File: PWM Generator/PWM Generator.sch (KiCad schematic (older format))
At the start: 7 parts

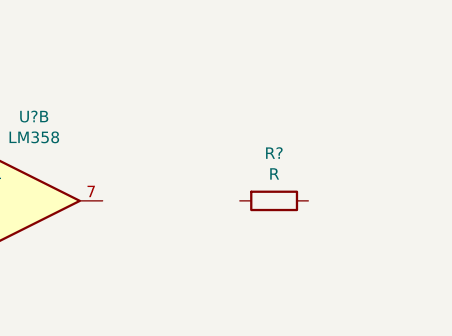
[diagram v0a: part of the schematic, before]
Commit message: Add Diod
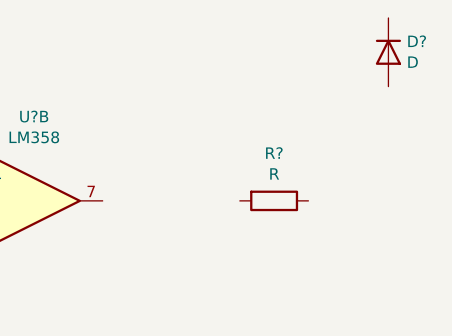
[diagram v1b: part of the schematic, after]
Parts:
- added D?: D, symbol Device:D
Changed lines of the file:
@@
+	0    1    1    0
+$EndComp
+$Comp
+L Device:D D?
+U 1 1 6A953FCE
+P 7900 1000
+F 0 "D?" V 7854 1080 50  0000 L CNN
+F 1 "D" V 7945 1080 50  0000 L CNN
+F 2 "" H 7900 1000 50  0001 C CNN
+F 3 "~" H 7900 1000 50  0001 C CNN
+	1    7900 1000
 	0    1    1    0
 $EndComp

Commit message: wired connection
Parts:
- added C1: C, symbol Device:C
- added C2, C3: CP1, symbol Device:CP1
- added J1, J2: Screw_Terminal_01x02, symbol Connector:Screw_Terminal_01x02
- added Q1: IRF3205, Package_TO_SOT_THT:TO-220-3_Vertical, symbol Transistor_FET:IRF3205
- added RV1: R_POT, symbol Device:R_POT
- added unit 3 of U1
- added U2: LM7805_TO220, Package_TO_SOT_THT:TO-220-3_Vertical, symbol Regulator_Linear:LM7805_TO220
- gave numbers to parts that had none: 7
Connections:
- net at U1.1: now also R3.1, R4.1
- net at U1.2 (-): now also R4.2, U1.5 (+), C1.1
- net at U1.3 (+): now also R1.2, R2.1, R3.2
- net at U1.6 (-): now also RV1.2
- net at U1.7: now also R5.1
- net +12C: now reaches D1.1 (K)
- net +12C: now also C2.1, J1.2 (Pin_2), J2.1 (Pin_1), U2.1 (VI)
- net at D1.2 (A): now also J2.2 (Pin_2), Q1.2 (D)
- net +5V: now reaches R1.1
- net +5V: now also C3.1, RV1.1, U1.8 (V+), U2.3 (VO)
- net GND: now reaches R2.2
- net GND: now also C1.2, C2.2, C3.2, J1.1 (Pin_1), Q1.3 (S), RV1.3, U1.4 (V-), U2.2 (GND)
- net at R5.2: now also Q1.1 (G)
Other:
- moved on the sheet: D1, R1, R2, R3, R4, R5, U1A, U1B

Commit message: PCB net
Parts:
- C1: footprint (none) -> Capacitor_THT:C_Radial_D6.3mm_H5.0mm_P2.50mm
- C2: footprint (none) -> Capacitor_THT:CP_Radial_D10.0mm_P3.50mm
- C3: footprint (none) -> Capacitor_THT:CP_Radial_D7.5mm_P2.50mm
- D1: footprint (none) -> Diode_THT:D_DO-27_P15.24mm_Horizontal
- J1, J2: footprint (none) -> TerminalBlock_4Ucon:TerminalBlock_4Ucon_1x02_P3.50mm_Horizontal
- R1: footprint (none) -> Resistor_THT:R_Radial_Power_L16.1mm_W9.0mm_P7.37mm
- R2, R4, R5: footprint (none) -> Resistor_THT:R_Radial_Power_L11.0mm_W7.0mm_P5.00mm
- R3: footprint (none) -> Resistor_THT:R_Radial_Power_L13.0mm_W9.0mm_P5.00mm
- RV1: footprint (none) -> Potentiometer_THT:Potentiometer_Runtron_RM-065_Vertical
- U1: footprint (none) -> Package_DIP:DIP-8_W7.62mm
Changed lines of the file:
@@
 F 0 "U1" H 3600 2867 50  0000 C CNN
 F 1 "LM358" H 3600 2776 50  0000 C CNN
-F 2 "" H 3600 2500 50  0001 C CNN
+F 2 "Package_DIP:DIP-8_W7.62mm" H 3600 2500 50  0001 C CNN
 F 3 "http://www.ti.com/lit/ds/symlink/lm2904-n.pdf" H 3600 2500 50  0001 C CNN
 	1    3600 2500
@@
 F 0 "U1" H 6150 2767 50  0000 C CNN
 F 1 "LM358" H 6150 2676 50  0000 C CNN
-F 2 "" H 6150 2400 50  0001 C CNN
+F 2 "Package_DIP:DIP-8_W7.62mm" H 6150 2400 50  0001 C CNN
 F 3 "http://www.ti.com/lit/ds/symlink/lm2904-n.pdf" H 6150 2400 50  0001 C CNN
 	2    6150 2400
@@
 F 0 "R4" H 3920 2846 50  0000 L CNN
 F 1 "R" H 3920 2755 50  0000 L CNN
-F 2 "" V 3780 2800 50  0001 C CNN
+F 2 "Resistor_THT:R_Radial_Power_L11.0mm_W7.0mm_P5.00mm" V 3780 2800 50  0001 C CNN
 F 3 "~" H 3850 2800 50  0001 C CNN
 	1    3850 2800
@@
 F 0 "R1" H 2520 2596 50  0000 L CNN
 F 1 "R" H 2520 2505 50  0000 L CNN
-F 2 "" V 2380 2550 50  0001 C CNN
+F 2 "Resistor_THT:R_Radial_Power_L16.1mm_W9.0mm_P7.37mm" V 2380 2550 50  0001 C CNN
 F 3 "~" H 2450 2550 50  0001 C CNN
 	1    2450 2550
@@
 F 0 "R2" H 2520 3146 50  0000 L CNN
 F 1 "R" H 2520 3055 50  0000 L CNN
-F 2 "" V 2380 3100 50  0001 C CNN
+F 2 "Resistor_THT:R_Radial_Power_L11.0mm_W7.0mm_P5.00mm" V 2380 3100 50  0001 C CNN
 F 3 "~" H 2450 3100 50  0001 C CNN
 	1    2450 3100
@@
 F 0 "R5" H 6870 2446 50  0000 L CNN
 F 1 "R" H 6870 2355 50  0000 L CNN
-F 2 "" V 6730 2400 50  0001 C CNN
+F 2 "Resistor_THT:R_Radial_Power_L11.0mm_W7.0mm_P5.00mm" V 6730 2400 50  0001 C CNN
 F 3 "~" H 6800 2400 50  0001 C CNN
 	1    6800 2400
@@
 F 0 "R3" V 2793 2150 50  0000 C CNN
 F 1 "R" V 2884 2150 50  0000 C CNN
-F 2 "" V 2930 2150 50  0001 C CNN
+F 2 "Resistor_THT:R_Radial_Power_L13.0mm_W9.0mm_P5.00mm" V 2930 2150 50  0001 C CNN
 F 3 "~" H 3000 2150 50  0001 C CNN
 	1    3000 2150
@@
 F 0 "D1" V 7404 1880 50  0000 L CNN
 F 1 "D" V 7495 1880 50  0000 L CNN
-F 2 "" H 7450 1800 50  0001 C CNN
+F 2 "Diode_THT:D_DO-27_P15.24mm_Horizontal" H 7450 1800 50  0001 C CNN
 F 3 "~" H 7450 1800 50  0001 C CNN
 	1    7450 1800
@@
 F 0 "C1" H 3315 3396 50  0000 L CNN
 F 1 "C" H 3315 3305 50  0000 L CNN
-F 2 "" H 3238 3200 50  0001 C CNN
+F 2 "Capacitor_THT:C_Radial_D6.3mm_H5.0mm_P2.50mm" H 3238 3200 50  0001 C CNN
 F 3 "~" H 3200 3350 50  0001 C CNN
 	1    3200 3350
@@
 F 0 "C2" H 3815 1396 50  0000 L CNN
 F 1 "CP1" H 3815 1305 50  0000 L CNN
-F 2 "" H 3700 1350 50  0001 C CNN
+F 2 "Capacitor_THT:CP_Radial_D10.0mm_P3.50mm" H 3700 1350 50  0001 C CNN
 F 3 "~" H 3700 1350 50  0001 C CNN
 	1    3700 1350
@@
 F 0 "C3" H 6465 1296 50  0000 L CNN
 F 1 "CP1" H 6465 1205 50  0000 L CNN
-F 2 "" H 6350 1250 50  0001 C CNN
+F 2 "Capacitor_THT:CP_Radial_D7.5mm_P2.50mm" H 6350 1250 50  0001 C CNN
 F 3 "~" H 6350 1250 50  0001 C CNN
 	1    6350 1250
@@
 F 0 "J2" H 9030 1692 50  0000 L CNN
 F 1 "Screw_Terminal_01x02" H 9030 1601 50  0000 L CNN
-F 2 "" H 8950 1700 50  0001 C CNN
+F 2 "TerminalBlock_4Ucon:TerminalBlock_4Ucon_1x02_P3.50mm_Horizontal" H 8950 1700 50  0001 C CNN
 F 3 "~" H 8950 1700 50  0001 C CNN
 	1    8950 1700
@@
 F 0 "J1" H 1518 1725 50  0000 C CNN
 F 1 "Screw_Terminal_01x02" H 1518 1816 50  0000 C CNN
-F 2 "" H 1600 2050 50  0001 C CNN
+F 2 "TerminalBlock_4Ucon:TerminalBlock_4Ucon_1x02_P3.50mm_Horizontal" H 1600 2050 50  0001 C CNN
 F 3 "~" H 1600 2050 50  0001 C CNN
 	1    1600 2050
@@
 F 0 "RV1" H 5081 2646 50  0000 R CNN
 F 1 "R_POT" H 5081 2555 50  0000 R CNN
-F 2 "" H 5150 2600 50  0001 C CNN
+F 2 "Potentiometer_THT:Potentiometer_Runtron_RM-065_Vertical" H 5150 2600 50  0001 C CNN
 F 3 "~" H 5150 2600 50  0001 C CNN
 	1    5150 2600
@@
 F 0 "U1" H 2108 2896 50  0000 L CNN
 F 1 "LM358" H 2108 2805 50  0000 L CNN
-F 2 "" H 2150 2850 50  0001 C CNN
+F 2 "Package_DIP:DIP-8_W7.62mm" H 2150 2850 50  0001 C CNN
 F 3 "http://www.ti.com/lit/ds/symlink/lm2904-n.pdf" H 2150 2850 50  0001 C CNN
 	3    2150 2850
